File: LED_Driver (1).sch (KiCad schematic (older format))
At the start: 6 parts, among them U2 AP5726

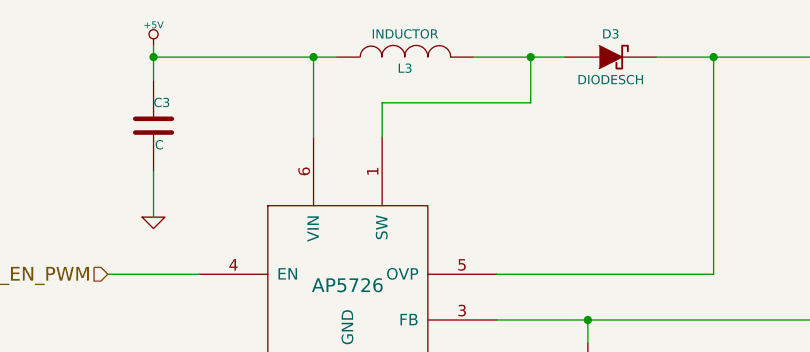
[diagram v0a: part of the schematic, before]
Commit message: Associate and Place Power Component
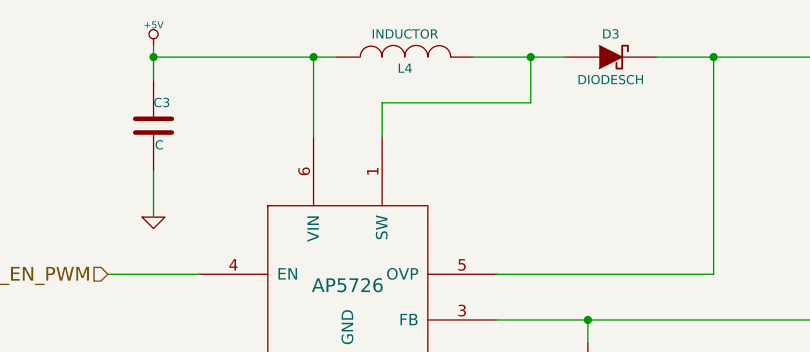
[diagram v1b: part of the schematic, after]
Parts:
- renumbered L3 to L4
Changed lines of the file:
@@
 	1200 1700 1600 1700
 $Comp
-L +5V #PWR18
+L +5V #PWR020
 U 1 1 52F2C07E
 P 1400 700
-F 0 "#PWR18" H 1400 790 20  0001 C CNN
+F 0 "#PWR020" H 1400 790 20  0001 C CNN
 F 1 "+5V" H 1400 790 30  0000 C CNN
 F 2 "" H 1400 700 60  0000 C CNN
@@
 	2100 750  2100 1100
 $Comp
-L GND #PWR19
+L GND #PWR021
 U 1 1 52F2C099
 P 1400 1450
-F 0 "#PWR19" H 1400 1450 30  0001 C CNN
+F 0 "#PWR021" H 1400 1450 30  0001 C CNN
 F 1 "GND" H 1400 1380 30  0001 C CNN
 F 2 "" H 1400 1450 60  0000 C CNN
@@
 Connection ~ 1400 750
 $Comp
-L INDUCTOR L3
+L INDUCTOR L4
 U 1 1 52F2C0D7
 P 2500 750
-F 0 "L3" V 2450 750 40  0000 C CNN
+F 0 "L4" V 2450 750 40  0000 C CNN
 F 1 "INDUCTOR" V 2600 750 40  0000 C CNN
 F 2 "~" H 2500 750 60  0000 C CNN
@@
 	2250 2350 2250 2700
 $Comp
-L GND #PWR20
+L GND #PWR022
 U 1 1 52F2C179
 P 2250 2700
-F 0 "#PWR20" H 2250 2700 30  0001 C CNN
+F 0 "#PWR022" H 2250 2700 30  0001 C CNN
 F 1 "GND" H 2250 2630 30  0001 C CNN
 F 2 "" H 2250 2700 60  0000 C CNN
@@
 Connection ~ 3850 750
 $Comp
-L GND #PWR21
+L GND #PWR023
 U 1 1 52F2CFAE
 P 9550 1750
-F 0 "#PWR21" H 9550 1750 30  0001 C CNN
+F 0 "#PWR023" H 9550 1750 30  0001 C CNN
 F 1 "GND" H 9550 1680 30  0001 C CNN
 F 2 "" H 9550 1750 60  0000 C CNN
